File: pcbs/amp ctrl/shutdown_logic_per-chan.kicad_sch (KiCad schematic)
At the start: 30 parts

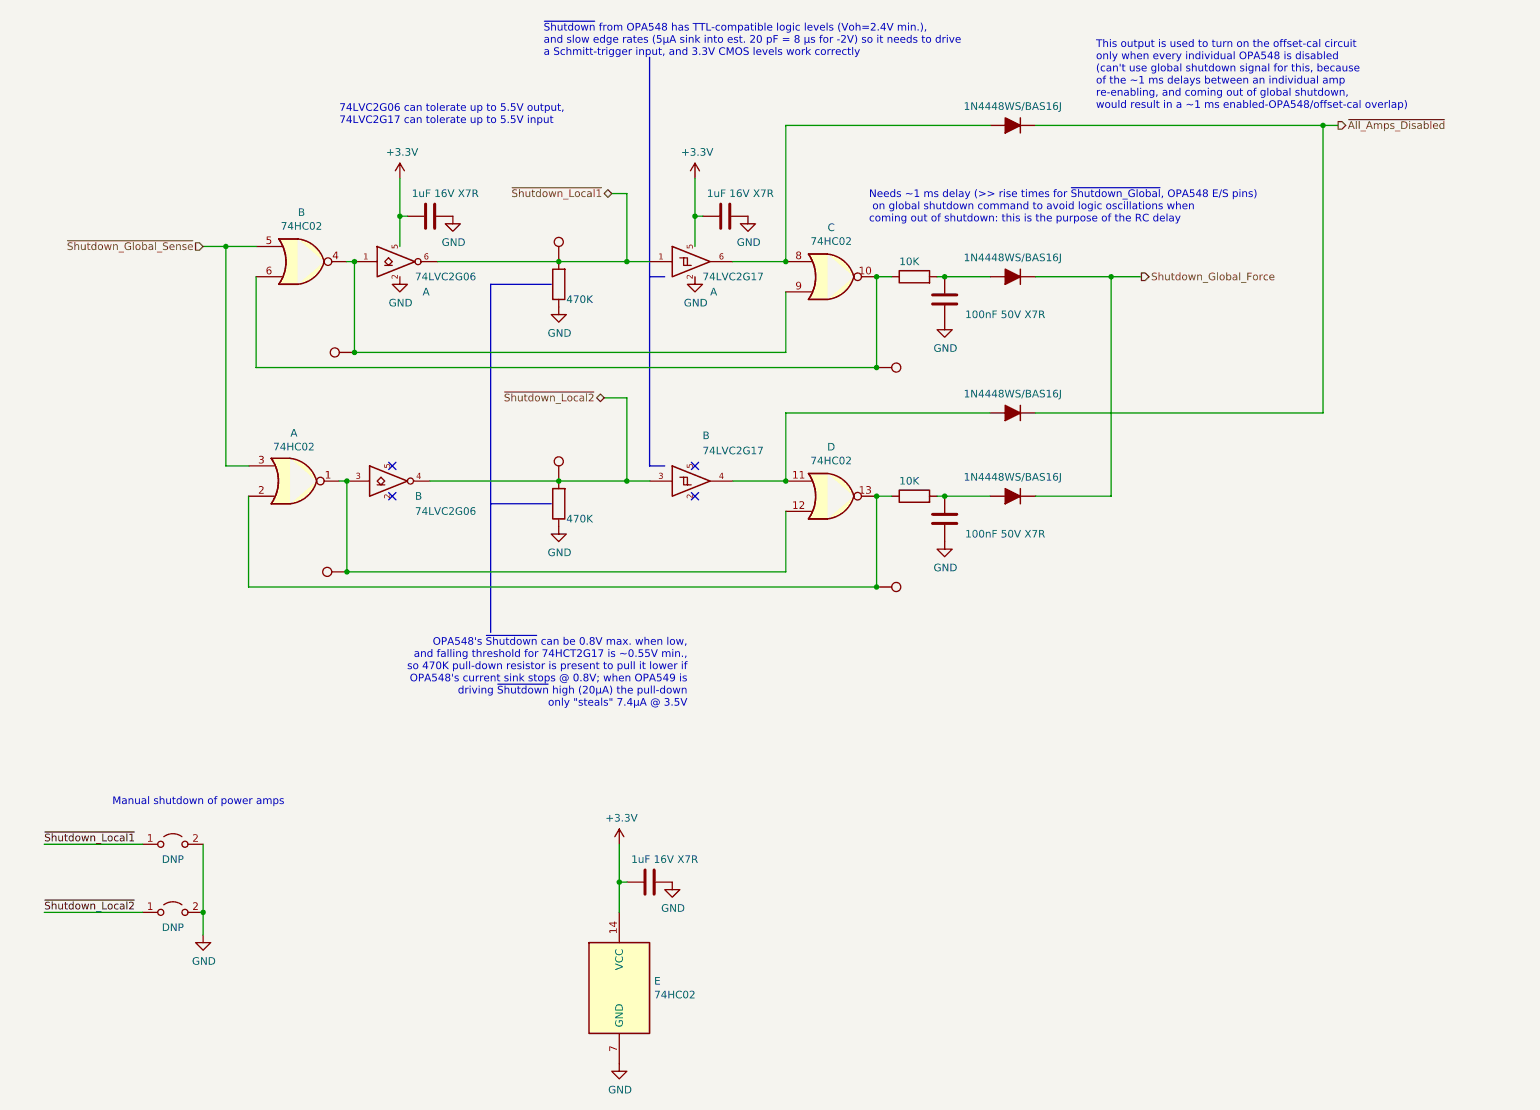
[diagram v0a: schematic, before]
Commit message: Schematic file fix, misc. PCB
Fixed issue with KiCAD's automatic V5→V6 migration (corrected in 6.0.11) that caused problems with component references in multi-channel schematic sheets
Finished migration in amp ctrl PCB, inc. re-assigning "exclude from BOM" attributes to testpoints, solder jumpers
Added mounting hole to amp ctrl PCB for addl support to Ethernet jacks, power connector through stiffener
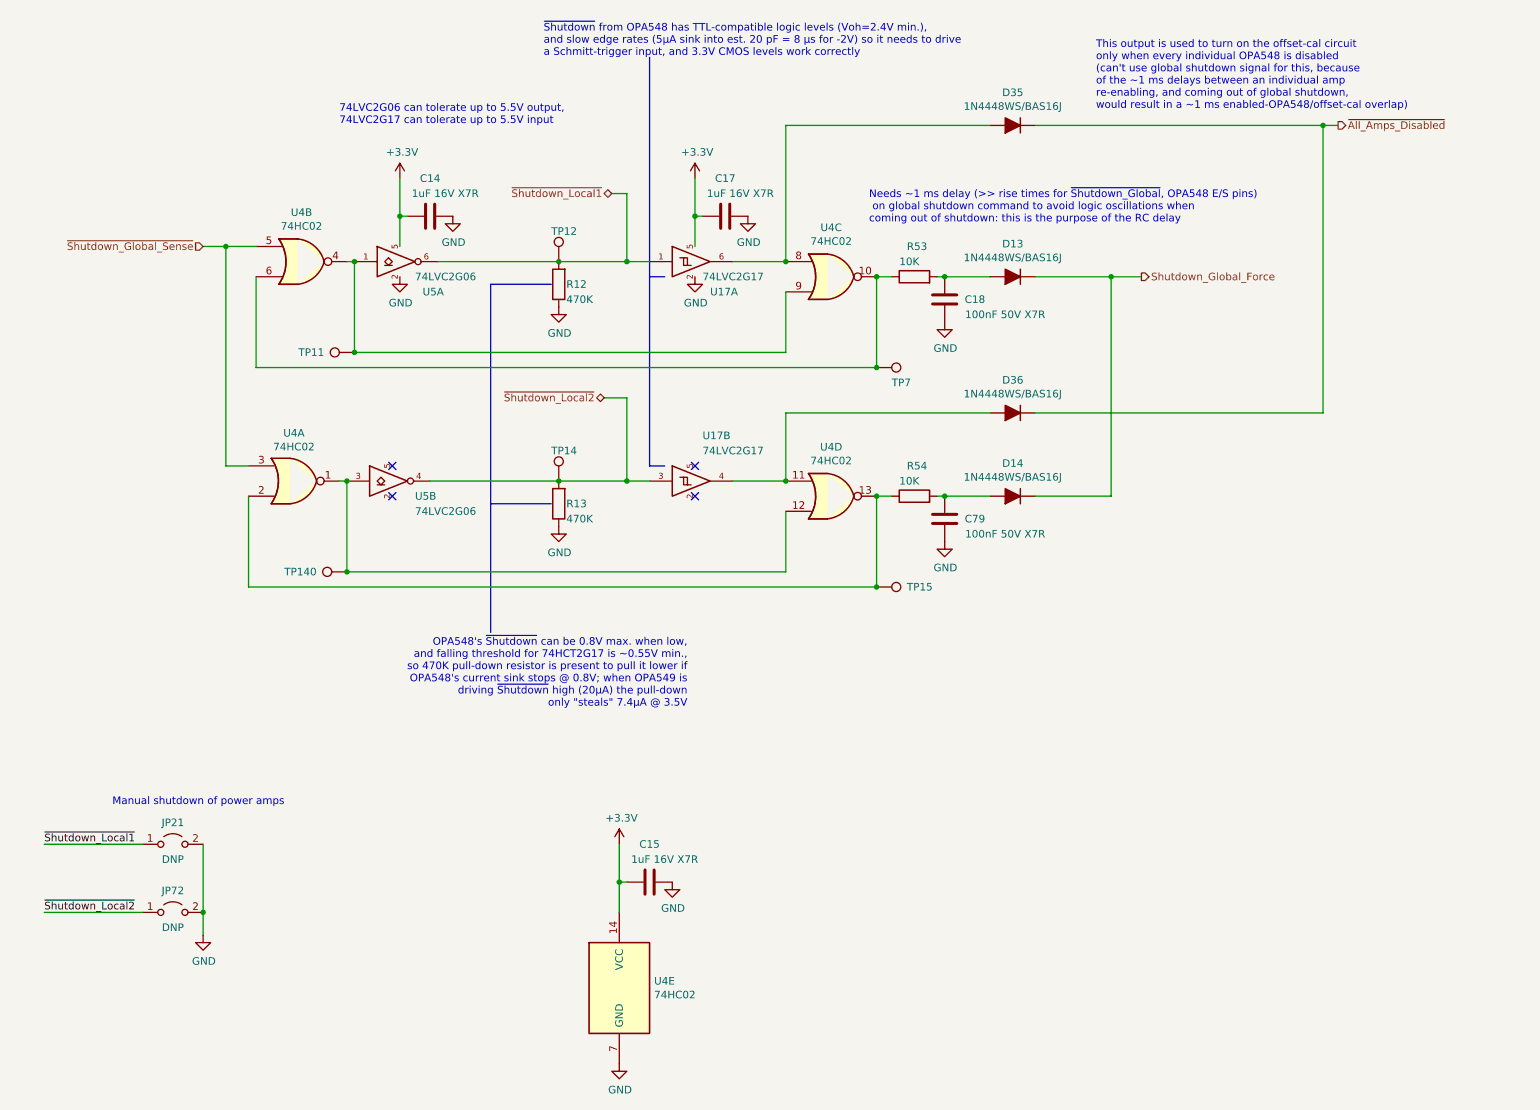
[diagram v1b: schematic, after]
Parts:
- gave numbers to parts that had none: 24

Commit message: Manufacturing fixes for amp control board
Arranged *.Fab text for assembly drawings
Minor stiffener outline fixes, silkscreen fixes
Fixed missing BOM fields on some parts
Removed exported manufacturing files from version control
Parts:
- D13, D14, D35, D36: Type (none) -> SMT
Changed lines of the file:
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@@
 (kicad_sch (version 20211123) (generator eeschema)
   (paper "A4")
+  (title_block
+    (date "2023-05-04")
+    (rev "D4")
+  )
   (junction (at 186.69 95.25) (diameter 0) (color 0 0 0 0)
   )
@@
       (effects (font (size 1.27 1.27)) hide)
     )
+    (property "Type" "SMT" (id 8) (at 209.55 58.42 0)
+      (effects (font (size 1.27 1.27)) hide)
+    )
     (pin "1")
     (pin "2")
@@
       (effects (font (size 1.27 1.27)) hide)
     )
+    (property "Type" "SMT" (id 8) (at 209.55 95.25 0)
+      (effects (font (size 1.27 1.27)) hide)
+    )
     (pin "1")
     (pin "2")
@@
       (effects (font (size 1.27 1.27)) hide)
     )
+    (property "Type" "SMT" (id 8) (at 209.55 33.02 0)
+      (effects (font (size 1.27 1.27)) hide)
+    )
     (pin "1")
     (pin "2")
@@
       (effects (font (size 1.27 1.27)) hide)
     )
+    (property "Type" "SMT" (id 8) (at 209.55 81.28 0)
+      (effects (font (size 1.27 1.27)) hide)
+    )

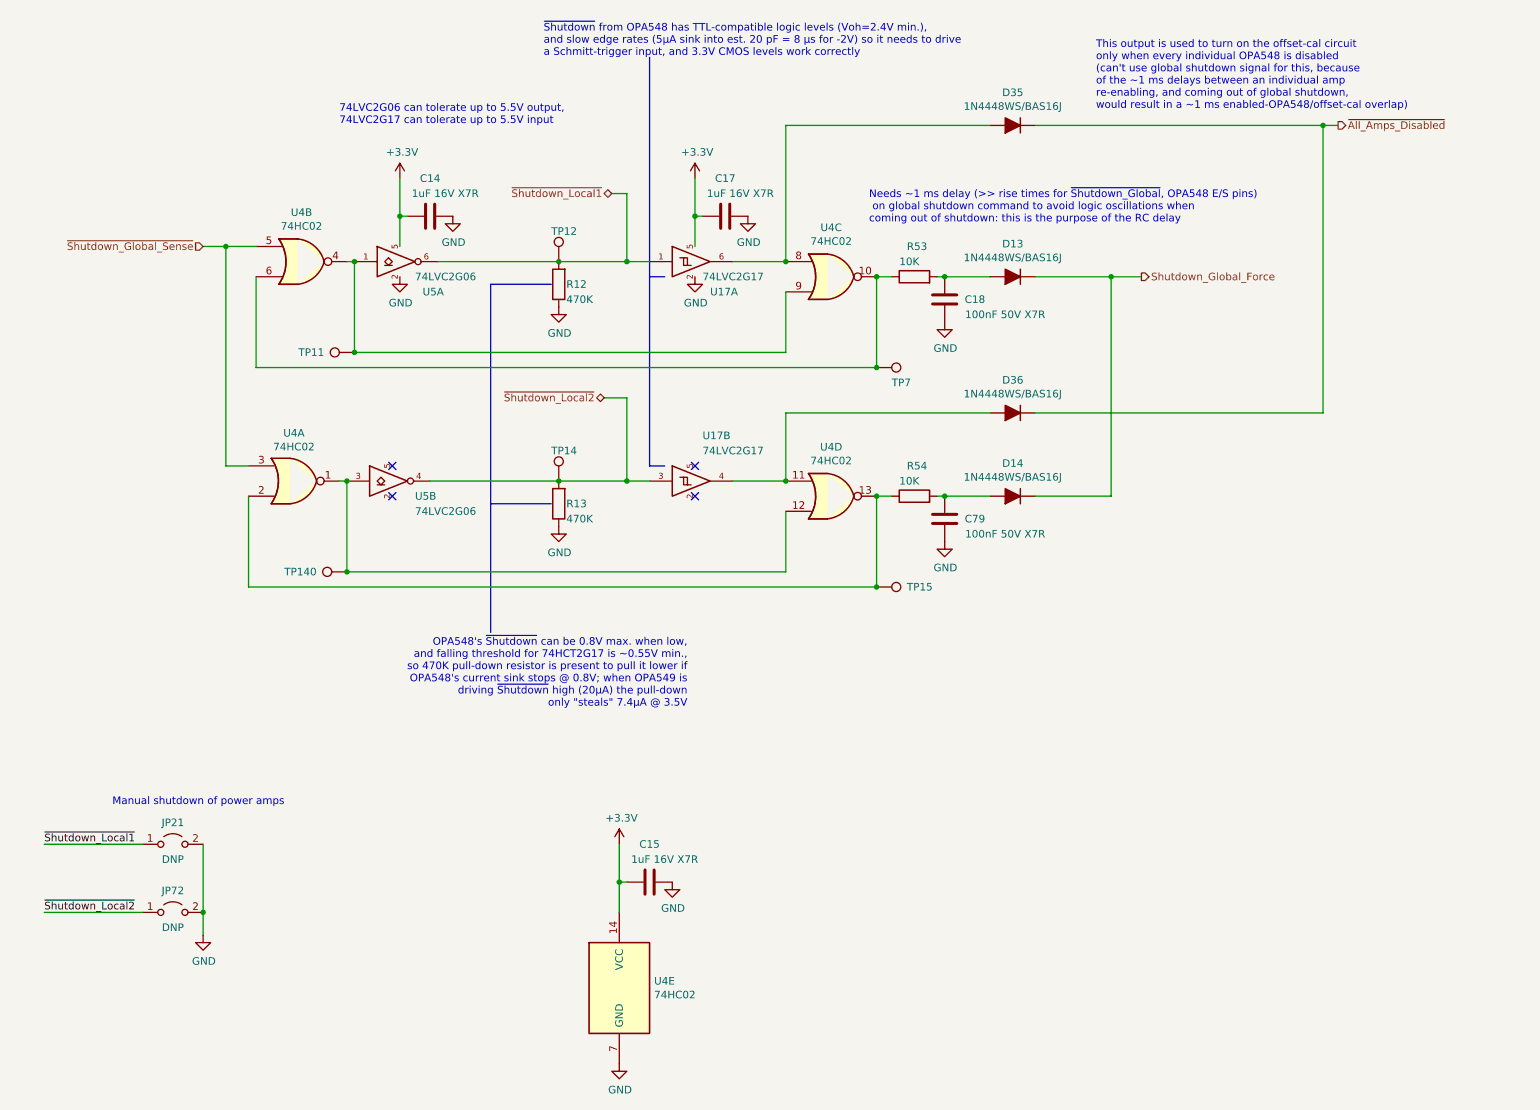
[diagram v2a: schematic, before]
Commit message: Upgraded to KiCAD 7.0 format Added 10µF cap to ADC's REFP pins to fix the voltage reference output (#15) Corrected ADC & DAC reset by adding a separate reset circuit (#14) Increased Cfbk compensation cap on each channel to work out-of-the-box with small coils (#16)
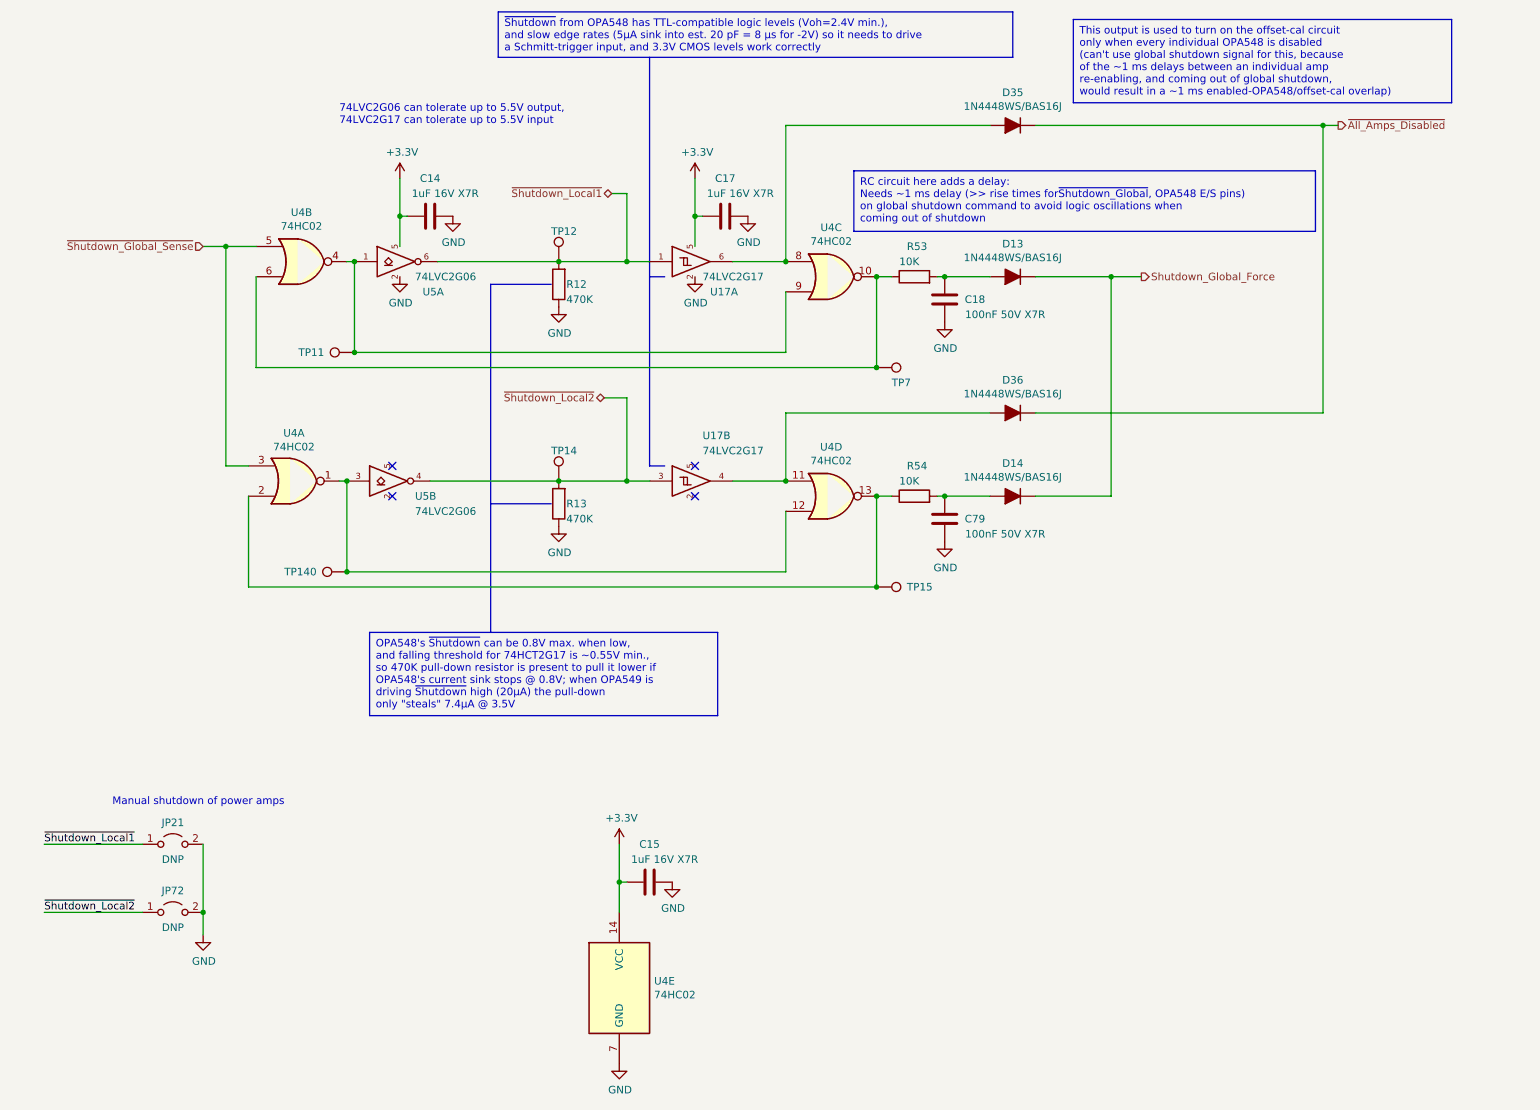
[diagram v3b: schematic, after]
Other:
- note removed: "Needs ~1 ms delay (>> rise times for ~{Shutdown_Global}, OPA548 E/S pins) on global shutdown command to avoid logic oscillations when coming out of shutdown: this is the purpose of the RC delay"
- note removed: "OPA548's ~{Shutdown} can be 0.8V max. when low, and falling threshold for 74HCT2G17 is ~0.55V min., so 470K pull-down resistor is present to pull it lower if OPA548's current sink stops @ 0.8V; when OPA549 is driving ~{Shutdown} high (20µA) the pull-down only "steals" 7.4µA @ 3.5V"
- note removed: "This output is used to turn on the offset-cal circuit only when every individual OPA548 is disabled (can't use global shutdown signal for this, because of the ~1 ms delays between an individual amp re-enabling, and coming out of global shutdown, would result in a ~1 ms enabled-OPA548/offset-cal overlap)"
- note removed: "~{Shutdown} from OPA548 has TTL-compatible logic levels (Voh=2.4V min.), and slow edge rates (5µA sink into est. 20 pF = 8 µs for -2V) so it needs to drive a Schmitt-trigger input, and 3.3V CMOS levels work correctly"

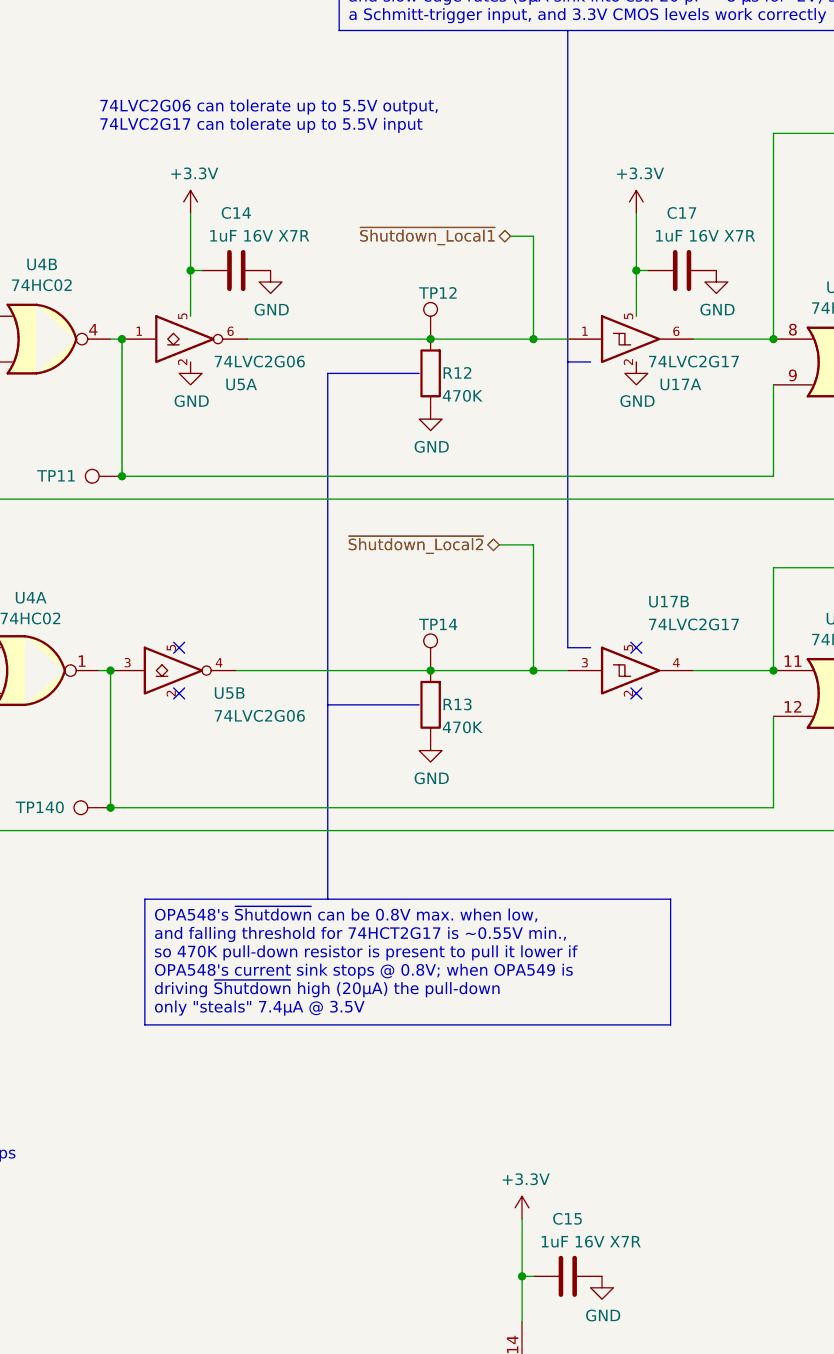
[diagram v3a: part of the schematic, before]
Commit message: Amp ctrl: lengthened ADC & DAC reset delay to ~50 ms (#14) Backplane: added clock multiplier for 10 Mhz scanner clock (fixes #21) Backplane: reduced R5 from 10 to 1 ohm, to avoid excessive voltage drop (#20) Backplane: replaced 15V regulator with efficient voltage limiter (#20) Backplane: changed all mounting holes to signal ground Backplane: replaced +2.5V regulator with a higher-current model to support FPGA I/O bank current draw Updated to KiCAD 8
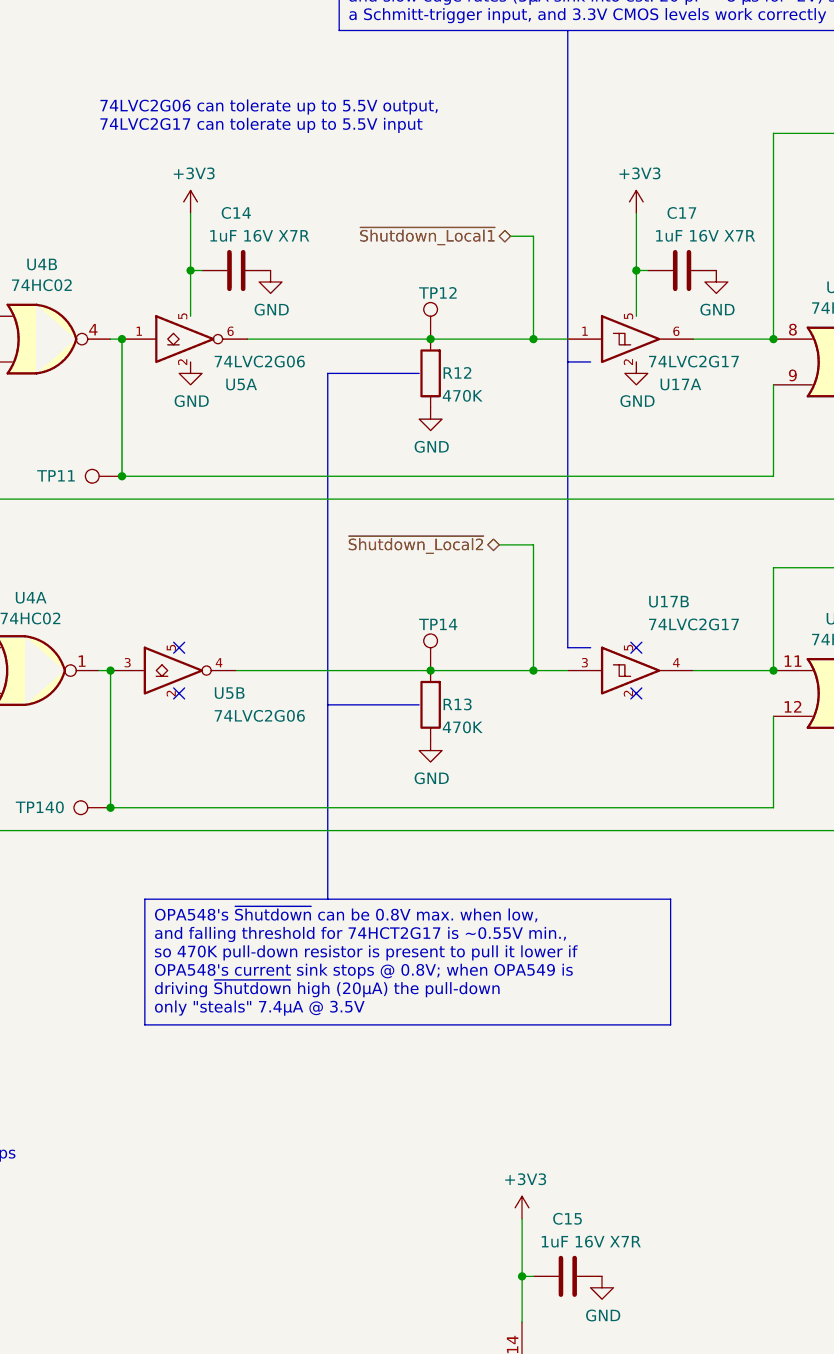
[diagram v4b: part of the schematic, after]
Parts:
- D13, D14, D35, D36: footprint Martinos_std:D_SOD-323F -> Don_std:D_SOD-323F
- R53, R54: Part Number RK73H2ATTD1002F -> RK73H2ATTE1002F
